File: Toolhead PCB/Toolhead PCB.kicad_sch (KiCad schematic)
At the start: 9 parts, among them J1 PicoA, J2 PicoB, J3 PicoC, J4 Heater, J5 Thermistor, J6 Heatbreak Fan, J7 Part Fan, J8 IR/ADXL, J9 MicroProbe

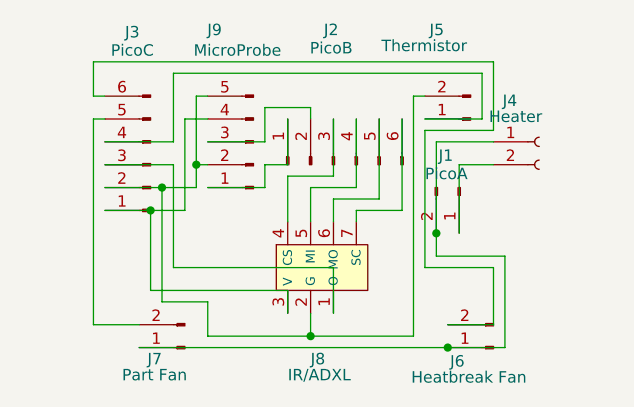
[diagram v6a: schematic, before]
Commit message: Labeled all the pins/nets. Moved connector Values to F.Silkscreen and moved connector References to F.Fab.
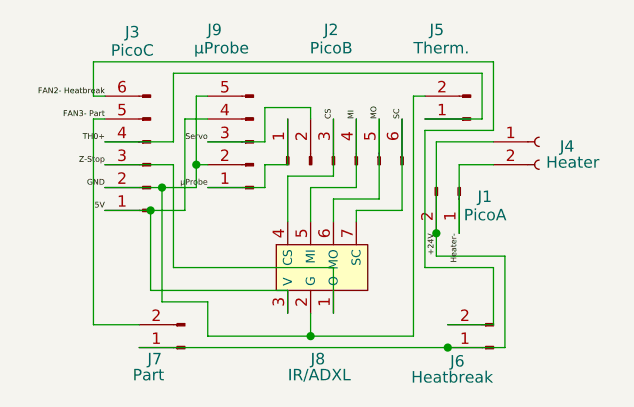
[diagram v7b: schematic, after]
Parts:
- J5: value Thermistor -> Therm.
- J6: value Heatbreak Fan -> Heatbreak
- J7: value Part Fan -> Part
- J9: value MicroProbe -> µProbe
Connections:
- net µProbe: now reaches J2.1 (Pin_1), J9.1 (Pin_1)
- net GND: now reaches J3.2 (Pin_2), J5.2 (Pin_2), J8.2 (G), J9.2 (Pin_2), J9.5 (Pin_5)
- net Servo: now reaches J2.2 (Pin_2), J9.3 (Pin_3)
- net 5V: now reaches J3.1 (Pin_1), J8.3 (V), J9.4 (Pin_4)
- net TH0+: now reaches J3.4 (Pin_4), J5.1 (Pin_1)
- net CS: now reaches J2.3 (Pin_3), J8.4 (CS)
- net MI: now reaches J2.4 (Pin_4), J8.5 (MI)
- net MO: now reaches J2.5 (Pin_5), J8.6 (MO)
- net SC: now reaches J2.6 (Pin_6), J8.7 (SC)
- net Heater-: now reaches J1.1 (Pin_1), J4.2 (Pin_2)
- net +24V: now reaches J1.2 (Pin_2), J4.1 (Pin_1), J6.1 (Pin_1), J7.1 (Pin_1)
- net FAN2- Heatbreak: now reaches J3.6 (Pin_6), J6.2 (Pin_2)
- net Z-Stop: now reaches J3.3 (Pin_3), J8.1 (O)
- net FAN3- Part: now reaches J3.5 (Pin_5), J7.2 (Pin_2)

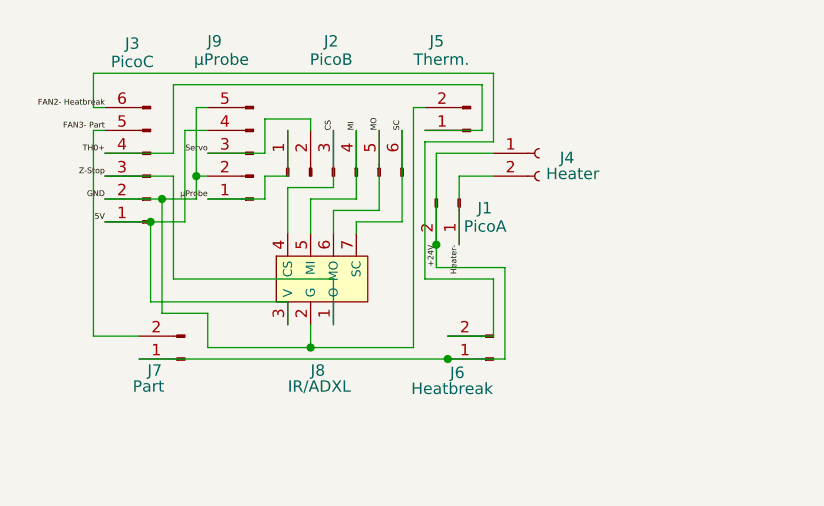
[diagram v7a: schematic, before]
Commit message: Redesigned PCB: - narrower so it does not protrude as much past the boundary when the Positron is packed for storage - all traces on front side only (no more manually soldered vias); still recommend fabricating as double-sided so the XT30 connector can be soldered on both sides - uses soldered wires to save space
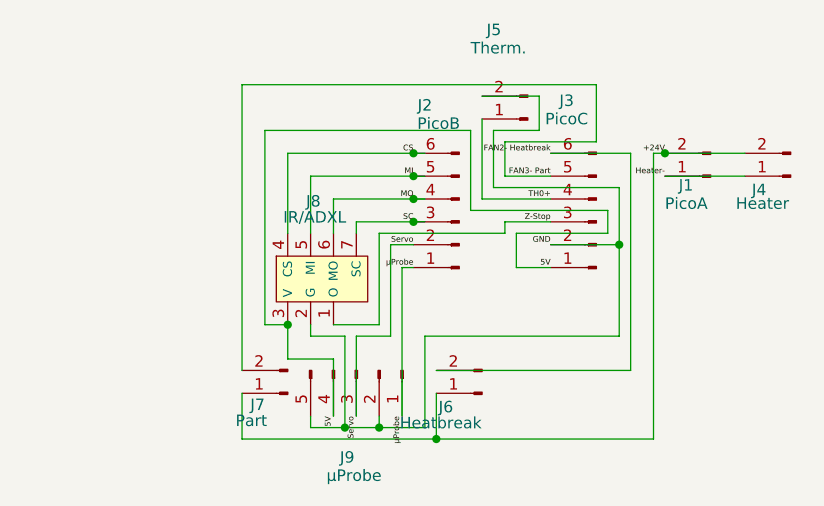
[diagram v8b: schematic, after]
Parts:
- J1: footprint TerminalBlock:TerminalBlock_Xinya_XY308-2.54-2P_1x02_P2.54mm_Horizontal -> Connector_Wire:SolderWire-0.5sqmm_1x02_P4.8mm_D0.9mm_OD2.3mm
- J4: footprint Connector_AMASS:AMASS_XT30PW-F_1x02_P2.50mm_Horizontal -> Connector_AMASS:AMASS_XT30UPB-M_1x02_P5.0mm_Vertical; symbol Connector:Conn_01x02_Socket -> Connector:Conn_01x02_Pin
- J5: footprint Connector_JST:JST_XH_B2B-XH-A_1x02_P2.50mm_Vertical -> Connector_JST:JST_XH_S2B-XH-A_1x02_P2.50mm_Horizontal
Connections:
- net +24V: now also J4.2 (Pin_2); no longer J4.1 (Pin_1)
- net CS: now also J2.6 (Pin_6); no longer J2.3 (Pin_3)
- net Heater-: now also J4.1 (Pin_1); no longer J4.2 (Pin_2)
- net MI: now also J2.5 (Pin_5); no longer J2.4 (Pin_4)
- net MO: now also J2.4 (Pin_4); no longer J2.5 (Pin_5)
- net SC: now also J2.3 (Pin_3); no longer J2.6 (Pin_6)
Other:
- moved on the sheet: J1, J2, J3, J5, J6, J7, J9
